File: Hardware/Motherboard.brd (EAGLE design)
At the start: 124.5 x 73.7 mm, 103 parts, among them J1 MICROMOD-2222-C, J10 MICRO-SD-PUSH-PUSH-EXT-PIN, J2 Vertical Qwiic Connector, J4 QWIIC_RIGHT_ANGLE, J5 CORTEX_JTAG_DEBUG_MINIMUM_PTH, J6 MICROMOD_CARRIER, J7 MICROMOD_CARRIER, Q1 3.1A/30V/105mΩ, U2 MCP73831, U5 AP7361C-33

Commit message: Removes old labels
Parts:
- removed U$25: (no value), top:#G1#PROCESSOR#517
- removed U$26: (no value), top:#G0#PROCESSOR#517
- removed U$27: (no value), top:#ALT_PWR_EN1#517
- removed U$28: (no value), top:#ALT_PWR_EN0#517
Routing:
- net 3.3V: track 243.7 -> 242.4 mm
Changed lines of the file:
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@@
 <?xml version="1.0" encoding="utf-8"?>
 <!DOCTYPE eagle SYSTEM "eagle.dtd">
-<eagle version="9.6.2">
+<eagle version="9.5.1">
 <drawing>
 <settings>
@@
 <setting verticaltext="up"/>
 </settings>
-<grid distance="0.01" unitdist="inch" unit="inch" style="dots" multiple="1" display="yes" altdistance="0.001" altunitdist="inch" altunit="inch"/>
+<grid distance="0.05" unitdist="inch" unit="inch" style="dots" multiple="1" display="yes" altdistance="0.005" altunitdist="inch" altunit="inch"/>
 <layers>
 <layer number="1" name="Top" color="4" fill="1" visible="yes" active="yes"/>
@@
 <attribute name="VALUE" x="6.985" y="18.288" size="0.6096" layer="27" font="vector" ratio="20" rot="R270" align="top-center"/>
 </element>
-<element name="U$25" library="top" package="#G1#PROCESSOR#517" value="" x="33.4264" y="42.7736" smashed="yes" rot="MR90"/>
-<element name="U$26" library="top" package="#G0#PROCESSOR#517" value="" x="29.1846" y="42.6466" smashed="yes" rot="MR90"/>
-<element name="U$27" library="top" package="#ALT_PWR_EN1#517" value="" x="34.7472" y="43.3578" smashed="yes" rot="MR90"/>
-<element name="U$28" library="top" package="#ALT_PWR_EN0#517" value="" x="30.5308" y="43.2562" smashed="yes" rot="MR90"/>
 <element name="J9" library="SparkFun-Connectors" package="1X03_LOCK" value="" x="31.242" y="63.5" smashed="yes">
 <attribute name="NAME" x="29.972" y="64.897" size="0.6096" layer="25" font="vector" ratio="20"/>
@@
 <via x="19.558" y="43.688" extent="1-16" drill="0.35"/>
 <via x="16.2052" y="43.688" extent="1-16" drill="0.35"/>
-<wire x1="33.02" y1="43.688" x2="38.1" y2="43.688" width="0.5588" layer="16"/>
 <wire x1="19.558" y1="43.688" x2="16.2052" y2="43.688" width="0.5588" layer="16"/>
 <via x="38.1" y="43.688" extent="1-16" drill="0.3048"/>
@@
 <vertex x="70.8406" y="67.5132"/>
 </polygon>
-<wire x1="108.458" y1="68.58" x2="104.394" y2="68.58" width="0.5588" layer="16"/>
-<wire x1="104.394" y1="68.58" x2="98.298" y2="68.58" width="0.5588" layer="16"/>
+<wire x1="108.458" y1="68.58" x2="98.298" y2="68.58" width="0.5588" layer="16"/>
 <wire x1="70.8152" y1="68.58" x2="70.8152" y2="67.0306" width="0.5588" layer="16"/>
 <via x="70.8152" y="67.0306" extent="1-16" drill="0.3048"/>
@@
 <wire x1="4.3688" y1="30.9871" x2="7.1891" y2="33.8074" width="0.2032" layer="1"/>
 <wire x1="7.1891" y1="33.8074" x2="10.7696" y2="33.8074" width="0.2032" layer="1"/>
-<wire x1="31.496" y1="42.164" x2="33.02" y2="43.688" width="0.5588" layer="16"/>
-<wire x1="19.558" y1="43.688" x2="25.146" y2="43.688" width="0.5588" layer="16"/>
-<wire x1="25.146" y1="43.688" x2="26.67" y2="42.164" width="0.5588" layer="16"/>
-<wire x1="26.67" y1="42.164" x2="31.496" y2="42.164" width="0.5588" layer="16"/>
+<wire x1="19.558" y1="43.688" x2="38.1" y2="43.688" width="0.5588" layer="16"/>
 </signal>
 <signal name="3.3V_EN">

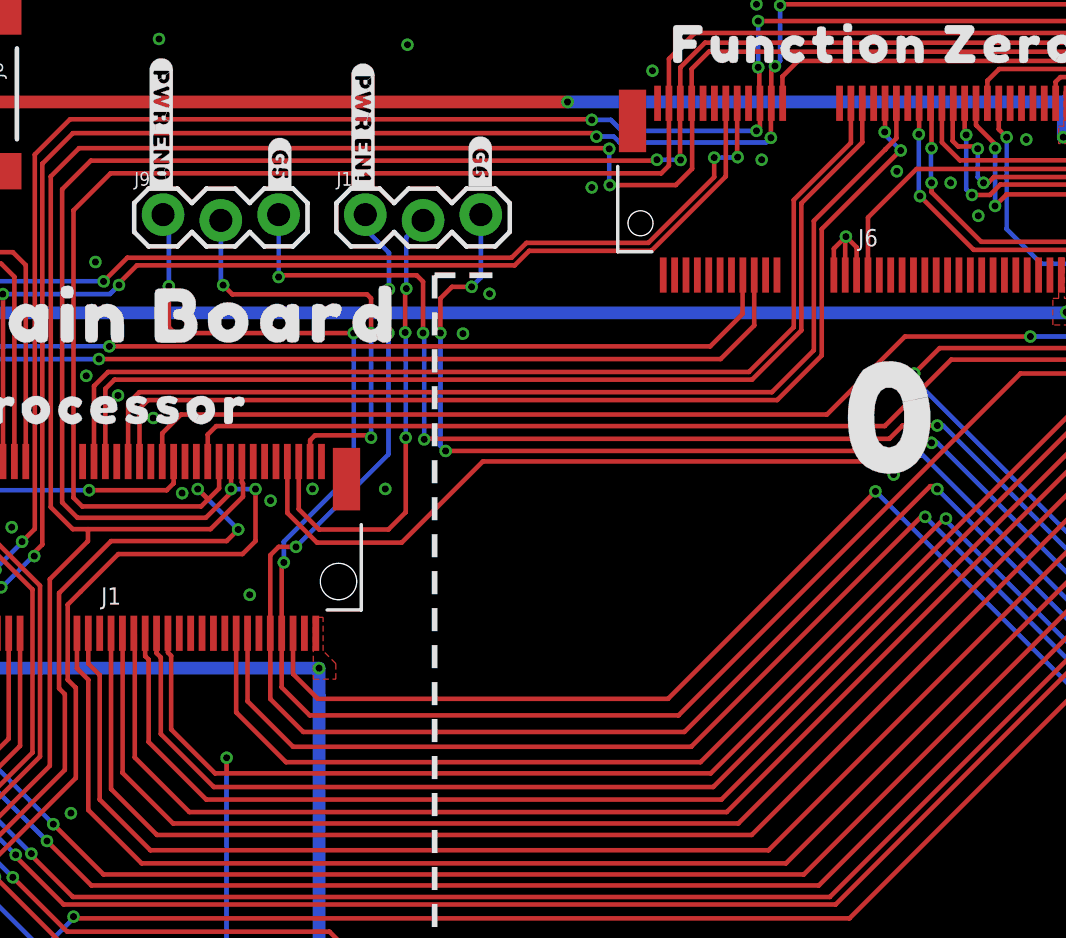
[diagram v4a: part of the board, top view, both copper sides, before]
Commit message: Moves labels, seeds more vias
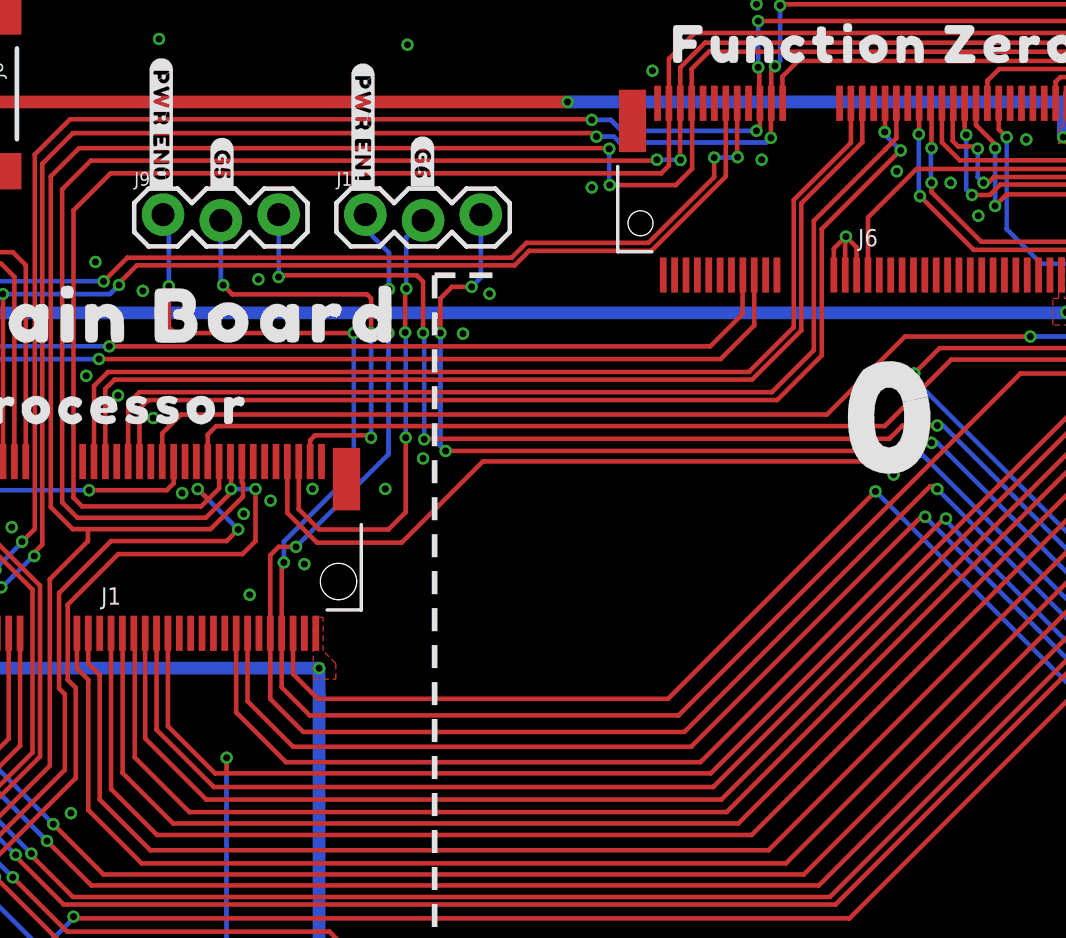
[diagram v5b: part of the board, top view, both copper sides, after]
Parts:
- moved U$29 2.54 mm to (42.6, 65.8)
- moved U$32 2.54 mm to (33.8, 65.8)
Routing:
- net GND: vias 76 -> 82

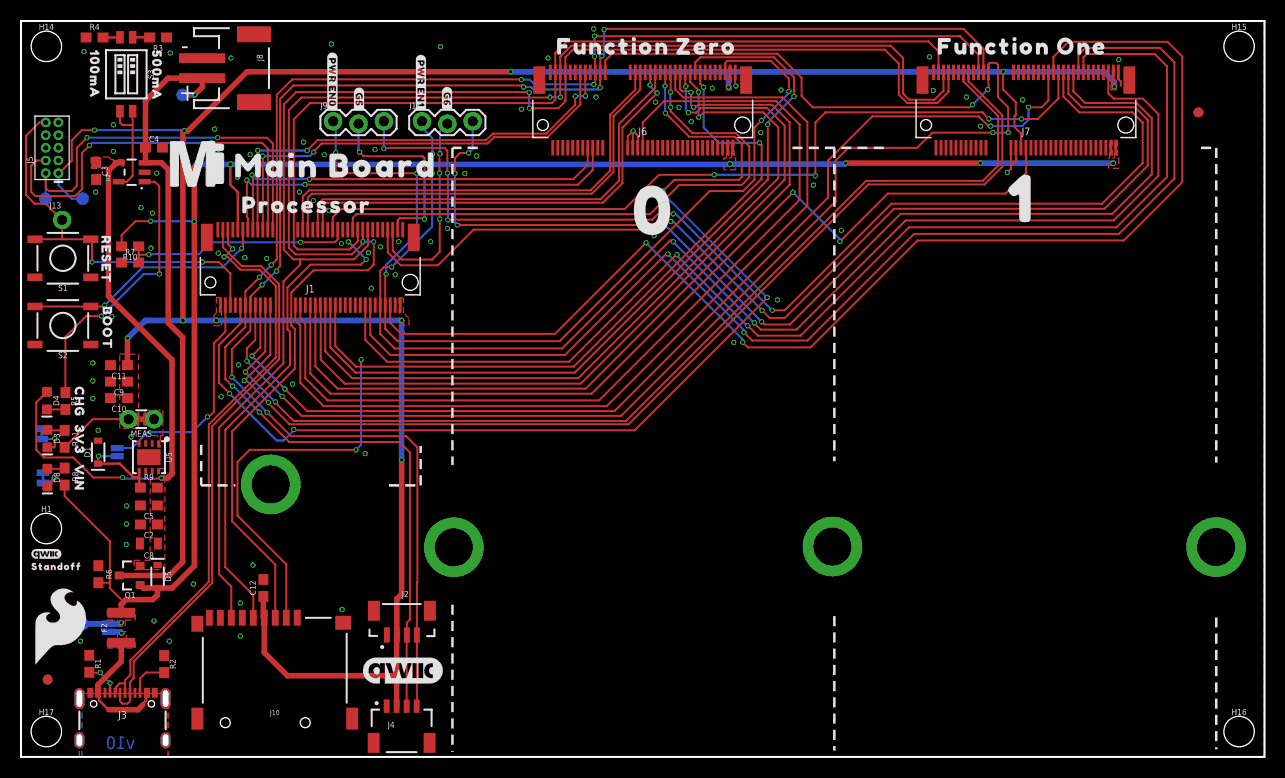
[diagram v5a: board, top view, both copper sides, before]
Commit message: Adds labels to pwr-enable selection headers, moves SD card slightly towards center of board
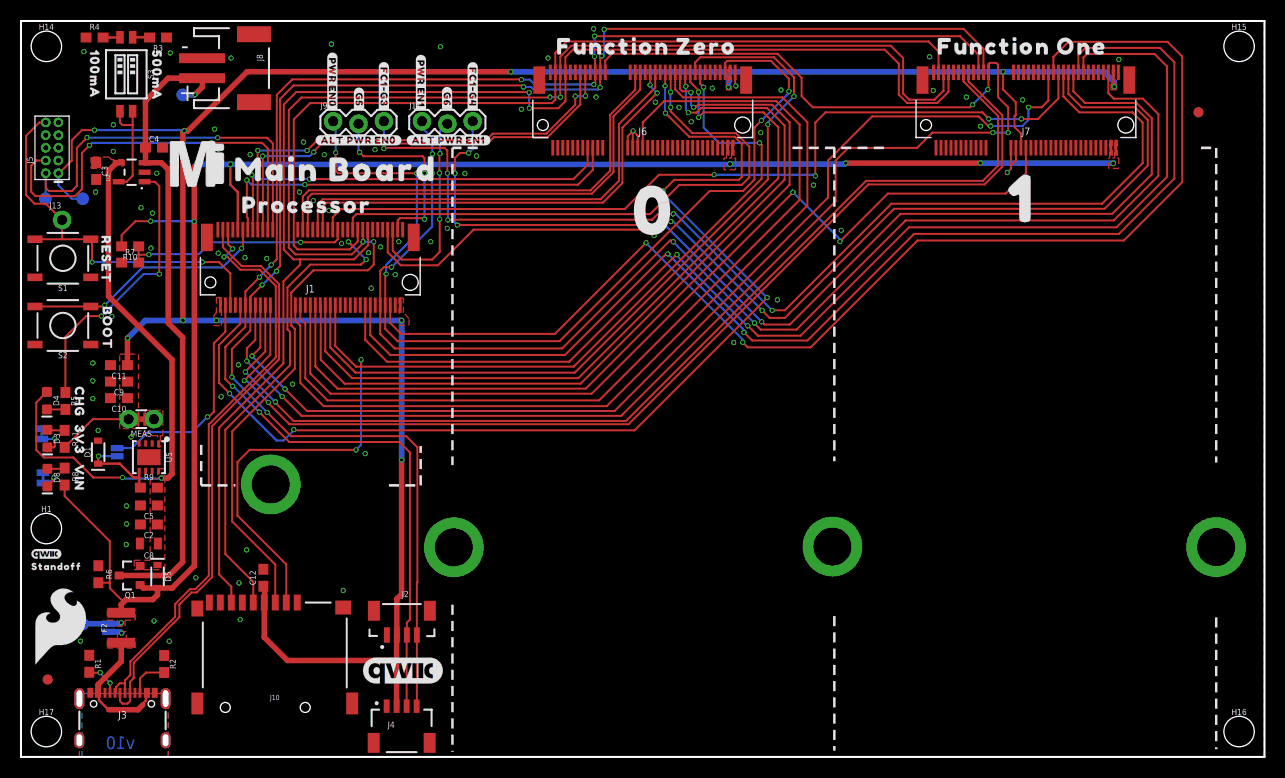
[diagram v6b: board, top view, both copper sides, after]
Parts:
- added U$25: (no value), top:#ALT_PWR_EN0#510
- added U$26: (no value), top:#ALT_PWR_EN1#510
- added U$27: (no value), top:#FC1#G3#518
- added U$28: (no value), top:#FC1#G4#518
- moved J10 1.52 mm to (25.4, 4.95)
- moved C12 1.02 mm to (24.3, 17.9)
- moved U$21 0.38 mm to (31.5, 58.8)
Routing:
- net SPI_PROCESSOR_SDI: track 145.4 -> 143.9 mm
- net SPI_PROCESSOR_SCK: track 142.9 -> 141.4 mm
- net G4-PROCESSOR/SD_CARD_!CS!: track 110.9 -> 109.3 mm
- net SPI_PROCESSOR_SDO: track 150.3 -> 148.8 mm
- net GND: track 13.0 -> 12.2 mm

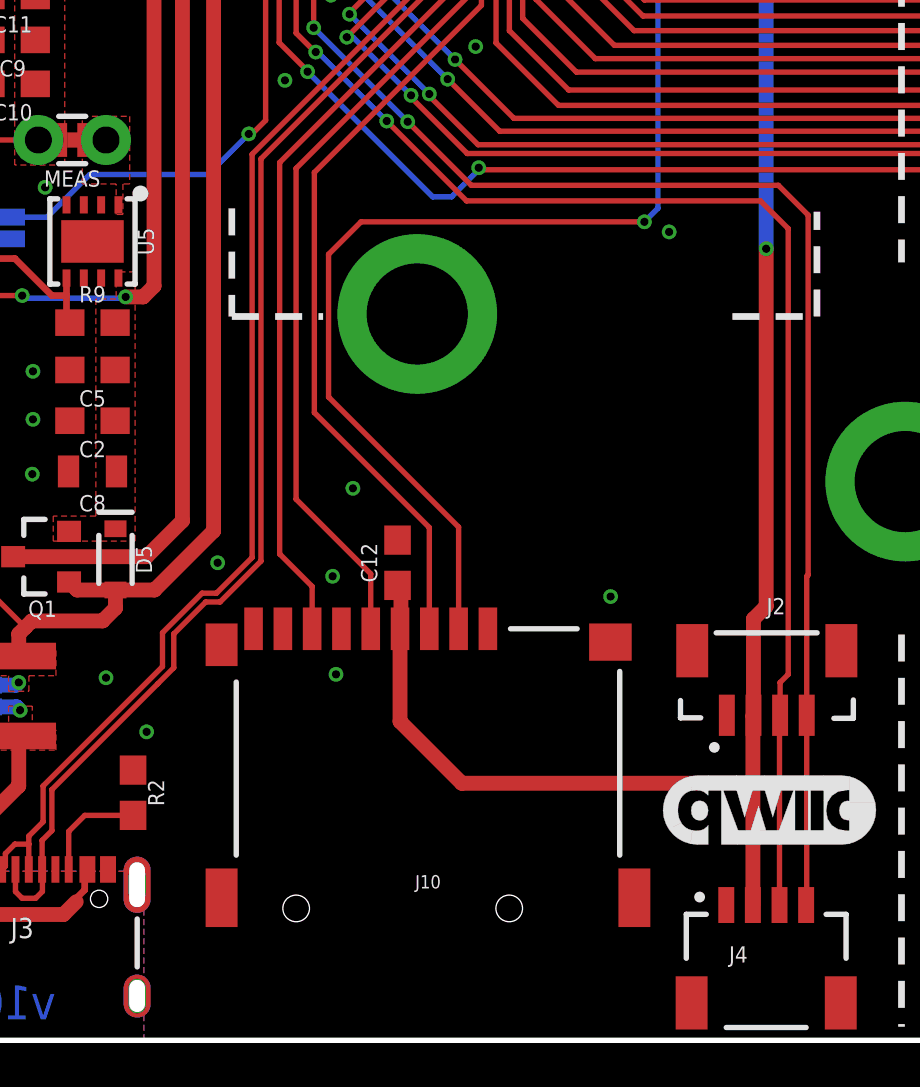
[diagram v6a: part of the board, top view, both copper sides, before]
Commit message: ...and again moves SD card slightly upward
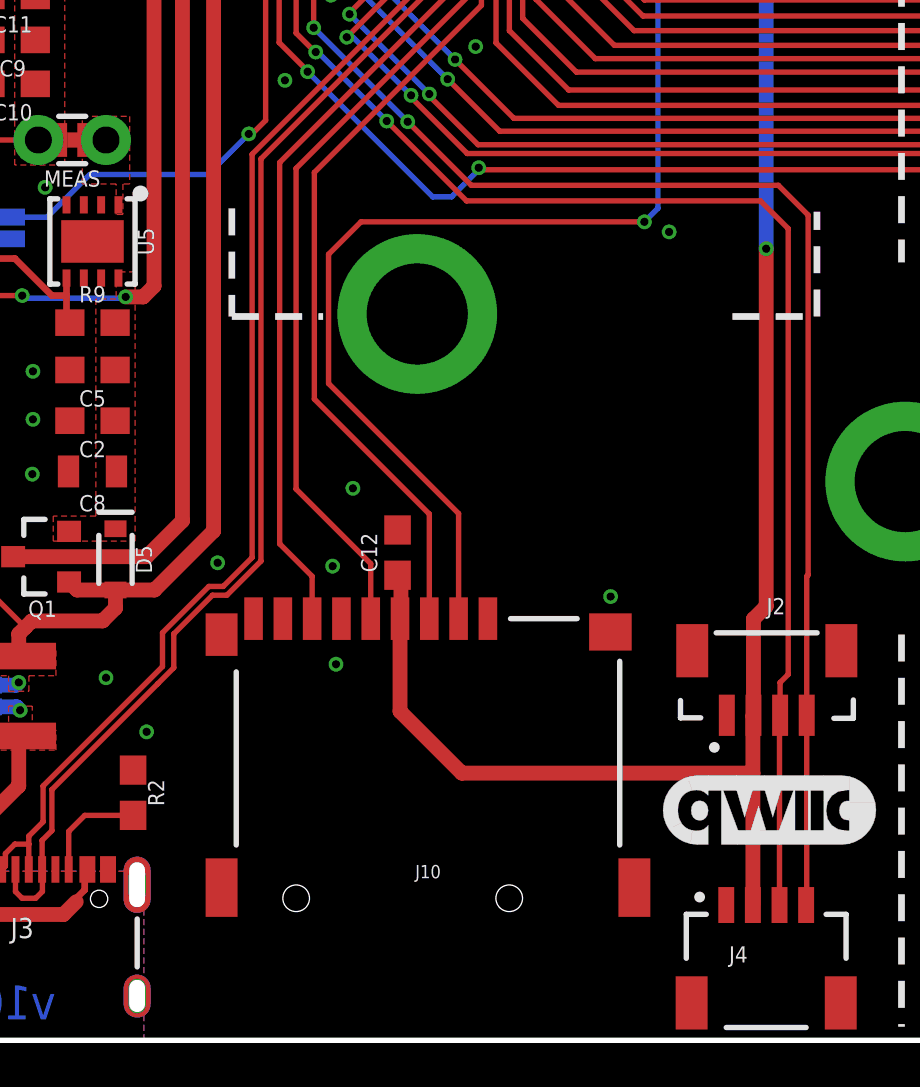
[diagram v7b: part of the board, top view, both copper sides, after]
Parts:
- moved C12 0.38 mm to (24.3, 18.3)
- moved J10 0.38 mm to (25.4, 5.33)

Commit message: Adds "Meas" silk
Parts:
- added U$33: (no value), top:#MEAS#40313513
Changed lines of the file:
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@@
 <setting verticaltext="up"/>
 </settings>
-<grid distance="0.02" unitdist="inch" unit="inch" style="dots" multiple="1" display="yes" altdistance="0.005" altunitdist="inch" altunit="inch"/>
+<grid distance="0.05" unitdist="inch" unit="inch" style="dots" multiple="1" display="yes" altdistance="0.005" altunitdist="inch" altunit="inch"/>
 <layers>
 <layer number="1" name="Top" color="4" fill="1" visible="yes" active="yes"/>
@@
 <element name="U$27" library="top" package="#FC1#G3#518" value="" x="36.322" y="67.056" smashed="yes" rot="R270"/>
 <element name="U$28" library="top" package="#FC1#G4#518" value="" x="45.212" y="67.056" smashed="yes" rot="R270"/>
+<element name="U$33" library="top" package="#MEAS#40313513" value="" x="14.732" y="34.671" smashed="yes" rot="R270"/>
 </elements>
 <signals>
